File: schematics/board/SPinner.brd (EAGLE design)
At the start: 71.4 x 71.4 mm, 9 parts

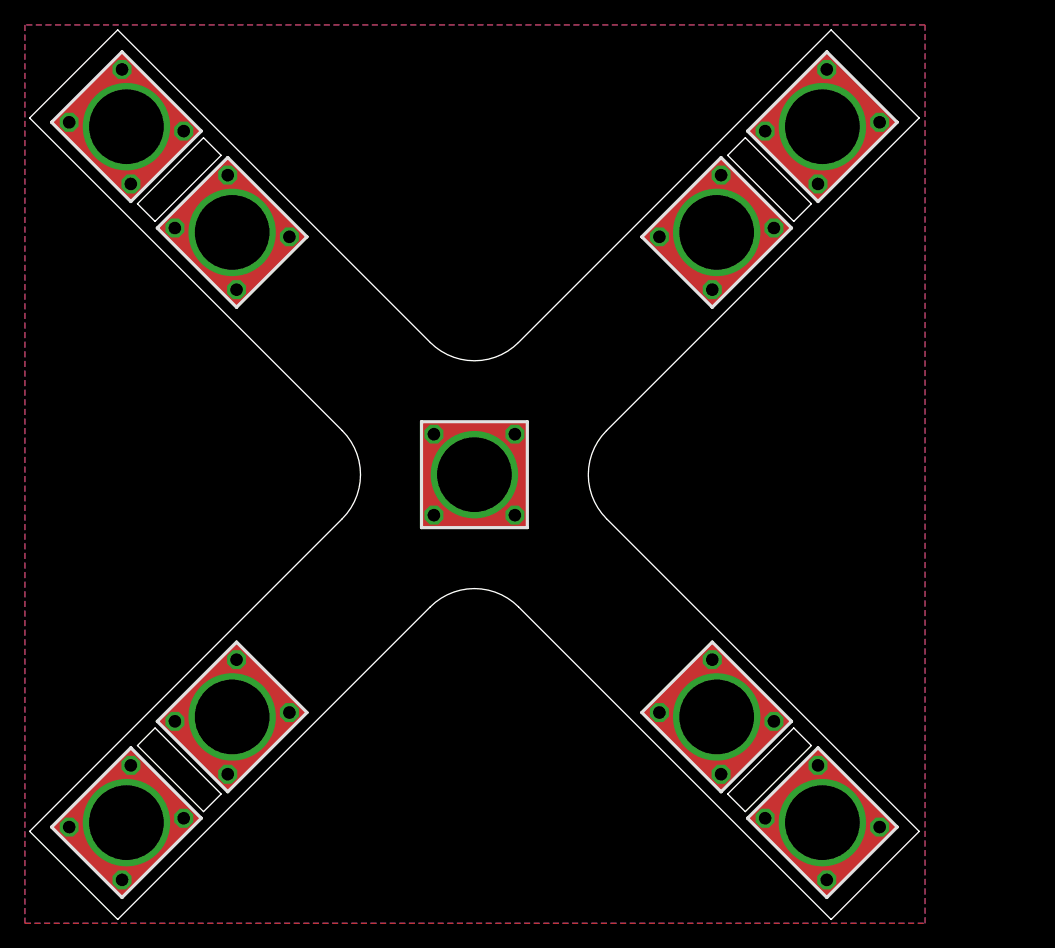
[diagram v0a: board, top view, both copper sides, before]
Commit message: Добавлены платы SP
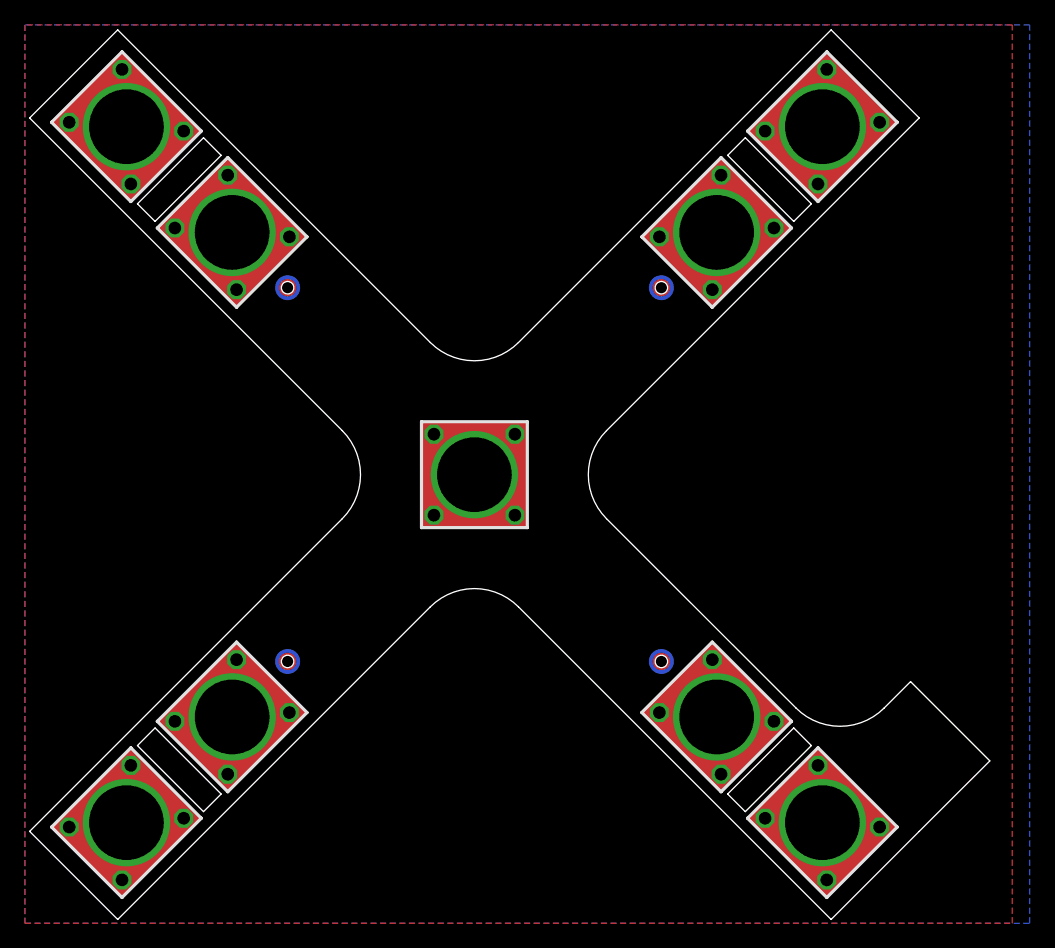
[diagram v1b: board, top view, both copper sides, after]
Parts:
- added U$6, U$7, U$8, U$9: GRAFIT-PASSIVE, CanCubeSat:GRAFIT-PASSIVE
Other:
- board size 71.4 x 71.4 mm -> 77.1 x 71.4 mm
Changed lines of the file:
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@@
 <drawing>
 <settings>
-<setting alwaysvectorfont="no"/>
+<setting alwaysvectorfont="yes"/>
 <setting verticaltext="up"/>
 </settings>
@@
 <wire x1="0" y1="7.071" x2="25.095" y2="32.166" width="0.1" layer="20"/>
 <wire x1="32.166" y1="25.095" x2="7.071" y2="0" width="0.1" layer="20"/>
-<wire x1="71.404" y1="7.071" x2="46.308" y2="32.166" width="0.1" layer="20"/>
+<wire x1="70.711" y1="19.092" x2="68.58811875" y2="16.96911875" width="0.1" layer="20"/>
+<wire x1="68.58811875" y1="16.96911875" x2="61.518465625" y2="16.96770625" width="0.1" layer="20" curve="-89.977084"/>
+<wire x1="61.518465625" y1="16.96770625" x2="46.308" y2="32.166" width="0.1" layer="20"/>
 <wire x1="39.237" y1="25.095" x2="64.333" y2="0" width="0.1" layer="20"/>
 <wire x1="7.071" y1="0" x2="0" y2="7.071" width="0.1" layer="20"/>
@@
 <wire x1="0" y1="64.333" x2="7.071" y2="71.404" width="0.1" layer="20"/>
 <wire x1="39.237" y1="46.308" x2="32.166" y2="46.308" width="0.1" layer="20" curve="-90"/>
+<wire x1="71.404" y1="7.071" x2="77.075" y2="12.728" width="0.1" layer="20"/>
+<wire x1="77.075" y1="12.728" x2="70.711" y2="19.092" width="0.1" layer="20"/>
 </plain>
 <attributes>
@@
 <attribute name="VALUE" x="32.162" y="29.257" size="1.27" layer="27"/>
 </element>
+<element name="U$6" library="CanCubeSat" package="GRAFIT-PASSIVE" value="GRAFIT-PASSIVE" x="20.709" y="20.709" smashed="yes" rot="R45"/>
+<element name="U$7" library="CanCubeSat" package="GRAFIT-PASSIVE" value="GRAFIT-PASSIVE" x="20.709" y="50.709" smashed="yes" rot="R315"/>
+<element name="U$8" library="CanCubeSat" package="GRAFIT-PASSIVE" value="GRAFIT-PASSIVE" x="50.709" y="20.709" smashed="yes" rot="R315"/>
+<element name="U$9" library="CanCubeSat" package="GRAFIT-PASSIVE" value="GRAFIT-PASSIVE" x="50.709" y="50.709" smashed="yes" rot="R45"/>
 </elements>
 <signals>
@@
 <vertex x="-0.3782" y="71.8028"/>
 <vertex x="-0.3782" y="-0.3072"/>
-<vertex x="71.8738" y="-0.3072"/>
-<vertex x="71.8738" y="71.8028"/>
+<vertex x="80.2738" y="-0.3072"/>
+<vertex x="80.2738" y="71.8028"/>
 </polygon>
 </signal>
@@
 <vertex x="-0.3782" y="71.8028"/>
 <vertex x="-0.3782" y="-0.3072"/>
-<vertex x="71.8738" y="-0.3072"/>
-<vertex x="71.8738" y="71.8028"/>
+<vertex x="78.8738" y="-0.3072"/>
+<vertex x="78.8738" y="71.8028"/>
 </polygon>
 </signal>

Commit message: Доделаны платы SP
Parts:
- added JP1: 1X02_EMPTY, CanCubeSat:1X02_EMPTY
- added U$10: BUTTON_6X6, CanCubeSat:BUTTON_6X6
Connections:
- new net N$1: JP1.1, U$10.P$2, U$10.P$3
- new net N$3: JP1.2, U$10.P$1, U$10.P$4
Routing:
- net N$1: track 0.00 -> 9.00 mm
- net N$3: track 0.00 -> 8.88 mm
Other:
- outline, holes or cut-outs redrawn
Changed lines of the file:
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@@
 <setting verticaltext="up"/>
 </settings>
-<grid distance="0.7" unitdist="mm" unit="mm" style="lines" multiple="1" display="yes" altdistance="0.01" altunitdist="mm" altunit="mm"/>
+<grid distance="0.2" unitdist="mm" unit="mm" style="lines" multiple="1" display="yes" altdistance="0.01" altunitdist="mm" altunit="mm"/>
 <layers>
 <layer number="1" name="Top" color="4" fill="1" visible="yes" active="yes"/>
@@
 <wire x1="0" y1="7.071" x2="25.095" y2="32.166" width="0.1" layer="20"/>
 <wire x1="32.166" y1="25.095" x2="7.071" y2="0" width="0.1" layer="20"/>
-<wire x1="70.711" y1="19.092" x2="68.58811875" y2="16.96911875" width="0.1" layer="20"/>
-<wire x1="68.58811875" y1="16.96911875" x2="61.518465625" y2="16.96770625" width="0.1" layer="20" curve="-89.977084"/>
-<wire x1="61.518465625" y1="16.96770625" x2="46.308" y2="32.166" width="0.1" layer="20"/>
+<wire x1="69.296" y1="20.506" x2="67.174003125" y2="18.383628125" width="0.1" layer="20"/>
+<wire x1="67.174003125" y1="18.383628125" x2="60.104153125" y2="18.3817875" width="0.1" layer="20" curve="-89.980275"/>
+<wire x1="60.104153125" y1="18.3817875" x2="46.308" y2="32.166" width="0.1" layer="20"/>
 <wire x1="39.237" y1="25.095" x2="64.333" y2="0" width="0.1" layer="20"/>
 <wire x1="7.071" y1="0" x2="0" y2="7.071" width="0.1" layer="20"/>
@@
 <wire x1="39.237" y1="46.308" x2="32.166" y2="46.308" width="0.1" layer="20" curve="-90"/>
 <wire x1="71.404" y1="7.071" x2="77.075" y2="12.728" width="0.1" layer="20"/>
-<wire x1="77.075" y1="12.728" x2="70.711" y2="19.092" width="0.1" layer="20"/>
+<wire x1="77.075" y1="12.728" x2="69.296" y2="20.506" width="0.1" layer="20"/>
 </plain>
 <attributes>
@@
 <element name="U$8" library="CanCubeSat" package="GRAFIT-PASSIVE" value="GRAFIT-PASSIVE" x="50.709" y="20.709" smashed="yes" rot="R315"/>
 <element name="U$9" library="CanCubeSat" package="GRAFIT-PASSIVE" value="GRAFIT-PASSIVE" x="50.709" y="50.709" smashed="yes" rot="R45"/>
+<element name="U$10" library="CanCubeSat" package="BUTTON_6X6" value="BUTTON_6X6" x="71" y="13" smashed="yes" rot="R135"/>
+<element name="JP1" library="CanCubeSat" package="1X02_EMPTY" value="1X02_EMPTY" x="67.2" y="16.6" smashed="yes" rot="R225">
+<attribute name="VALUE" x="66.7509875" y="20.641115625" size="1.27" layer="27" rot="R225"/>
+</element>
 </elements>
 <signals>
@@
 <wire x1="35.7" y1="35.7" x2="35.702" y2="35.702" width="0.8" layer="1"/>
 </signal>
+<signal name="N$1">
+<contactref element="U$10" pad="P$3"/>
+<contactref element="U$10" pad="P$2"/>
+<contactref element="JP1" pad="1"/>
+<wire x1="68.098025" y1="17.498025" x2="68.671609375" y2="16.924440625" width="0.8" layer="1"/>
+<wire x1="68.671609375" y1="16.924440625" x2="70.2575375" y2="16.924440625" width="0.8" layer="1"/>
+<wire x1="70.2575375" y1="16.924440625" x2="74.924440625" y2="12.2575375" width="0.8" layer="1"/>
+</signal>
+<signal name="N$3">
+<contactref element="U$10" pad="P$4"/>
+<contactref element="U$10" pad="P$1"/>
+<contactref element="JP1" pad="2"/>
+<wire x1="66.301971875" y1="15.701971875" x2="67.07555625" y2="14.9283875" width="0.8" layer="1"/>
+<wire x1="67.07555625" y1="14.9283875" x2="67.07555625" y2="13.742459375" width="0.8" layer="1"/>
+<wire x1="67.07555625" y1="13.742459375" x2="71.742459375" y2="9.07555625" width="0.8" layer="1"/>
+</signal>
 </signals>

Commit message: Проверил платы SPinner и SPin,внес декоративные правки
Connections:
- net BUS+1 renamed BUS+
- net N$2 renamed BUS-
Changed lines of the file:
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@@
 </elements>
 <signals>
-<signal name="BUS+1">
+<signal name="BUS+">
 <contactref element="U$1" pad="1"/>
 <contactref element="U$1" pad="2"/>
@@
 </polygon>
 </signal>
-<signal name="N$2">
+<signal name="BUS-">
 <contactref element="U$2" pad="1"/>
 <contactref element="U$2" pad="2"/>
